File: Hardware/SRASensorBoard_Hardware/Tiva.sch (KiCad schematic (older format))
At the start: 8 parts

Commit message: Added Okis to board
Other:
- moved on the sheet: U?C, U?D, U?G, U?H
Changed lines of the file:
@@
 L MRDT_Shields:TM4C129E_Launchpad U?
 U 3 1 614D9ED3
-P 6100 2150
-F 0 "U?" H 6050 3425 60  0000 L CNN
-F 1 "TM4C129E_Launchpad" H 5625 3300 60  0000 L CNN
-F 2 "" H 6100 2150 60  0001 C CNN
-F 3 "" H 6100 2150 60  0001 C CNN
-	3    6100 2150
+P 5425 2550
+F 0 "U?" H 5375 3825 60  0000 L CNN
+F 1 "TM4C129E_Launchpad" H 4950 3700 60  0000 L CNN
+F 2 "" H 5425 2550 60  0001 C CNN
+F 3 "" H 5425 2550 60  0001 C CNN
+	3    5425 2550
 	1    0    0    -1
 $EndComp
@@
 L MRDT_Shields:TM4C129E_Launchpad U?
 U 4 1 614DBFEF
-P 7425 2175
-F 0 "U?" H 7456 3452 60  0000 C CNN
-F 1 "TM4C129E_Launchpad" H 7456 3346 60  0000 C CNN
-F 2 "" H 7425 2175 60  0001 C CNN
-F 3 "" H 7425 2175 60  0001 C CNN
-	4    7425 2175
+P 6750 2575
+F 0 "U?" H 6781 3852 60  0000 C CNN
+F 1 "TM4C129E_Launchpad" H 6781 3746 60  0000 C CNN
+F 2 "" H 6750 2575 60  0001 C CNN
+F 3 "" H 6750 2575 60  0001 C CNN
+	4    6750 2575
 	-1   0    0    -1
 $EndComp
@@
 L MRDT_Shields:TM4C129E_Launchpad U?
 U 7 1 614E25CE
-P 6200 3775
-F 0 "U?" H 6200 5100 60  0000 L CNN
-F 1 "TM4C129E_Launchpad" H 5850 4950 60  0000 L CNN
-F 2 "" H 6200 3775 60  0001 C CNN
-F 3 "" H 6200 3775 60  0001 C CNN
-	7    6200 3775
+P 5525 4175
+F 0 "U?" H 5525 5500 60  0000 L CNN
+F 1 "TM4C129E_Launchpad" H 5175 5350 60  0000 L CNN
+F 2 "" H 5525 4175 60  0001 C CNN
+F 3 "" H 5525 4175 60  0001 C CNN
+	7    5525 4175
 	1    0    0    -1
 $EndComp
@@
 L MRDT_Shields:TM4C129E_Launchpad U?
 U 8 1 614E511C
-P 7450 3775
-F 0 "U?" H 7481 5052 60  0000 C CNN
-F 1 "TM4C129E_Launchpad" H 7481 4946 60  0000 C CNN
-F 2 "" H 7450 3775 60  0001 C CNN
-F 3 "" H 7450 3775 60  0001 C CNN
-	8    7450 3775
+P 6775 4175
+F 0 "U?" H 6806 5452 60  0000 C CNN
+F 1 "TM4C129E_Launchpad" H 6806 5346 60  0000 C CNN
+F 2 "" H 6775 4175 60  0001 C CNN
+F 3 "" H 6775 4175 60  0001 C CNN
+	8    6775 4175
 	-1   0    0    -1
 $EndComp
@@
 L power:GND #PWR?
 U 1 1 614FF513
-P 7775 2825
-F 0 "#PWR?" H 7775 2575 50  0001 C CNN
-F 1 "GND" V 7780 2697 50  0000 R CNN
-F 2 "" H 7775 2825 50  0001 C CNN
-F 3 "" H 7775 2825 50  0001 C CNN
-	1    7775 2825
+P 7100 3225
+F 0 "#PWR?" H 7100 2975 50  0001 C CNN
+F 1 "GND" V 7105 3097 50  0000 R CNN
+F 2 "" H 7100 3225 50  0001 C CNN
+F 3 "" H 7100 3225 50  0001 C CNN
+	1    7100 3225
 	0    -1   -1   0
 $EndComp
@@
 L power:GND #PWR?
 U 1 1 61500297
-P 7775 1225
-F 0 "#PWR?" H 7775 975 50  0001 C CNN
-F 1 "GND" V 7780 1097 50  0000 R CNN
-F 2 "" H 7775 1225 50  0001 C CNN
-F 3 "" H 7775 1225 50  0001 C CNN
-	1    7775 1225
+P 7100 1625
+F 0 "#PWR?" H 7100 1375 50  0001 C CNN
+F 1 "GND" V 7105 1497 50  0000 R CNN
+F 2 "" H 7100 1625 50  0001 C CNN
+F 3 "" H 7100 1625 50  0001 C CNN
+	1    7100 1625
 	0    -1   -1   0
 $EndComp
@@
 $EndComp
 Wire Wire Line
-	7625 1225 7775 1225
+	6950 1625 7100 1625
 Wire Wire Line
-	7650 2825 7775 2825
+	6975 3225 7100 3225
 Wire Wire Line
 	3825 3200 3950 3200

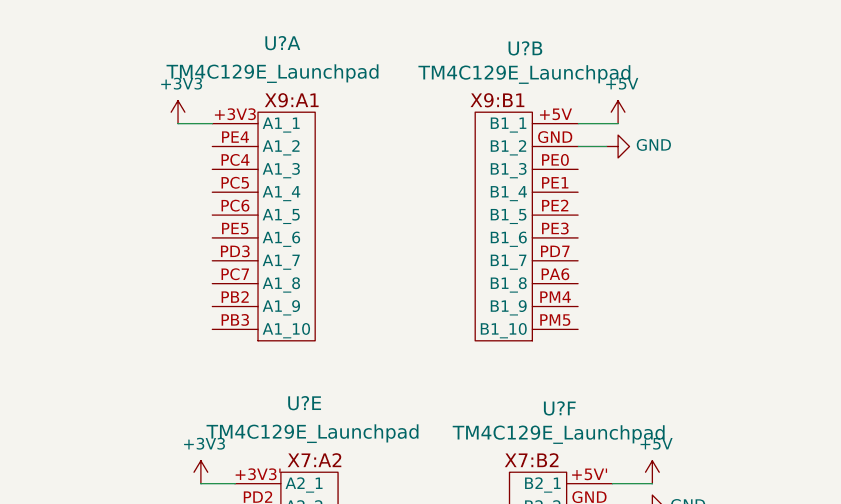
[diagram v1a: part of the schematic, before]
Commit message: Griffin_Buschjost_O2_Sensor
Copied in O2 Sensor from last year and added global labels to TIVA in pin 3 and 4 for the TIVA O2 RX and TX
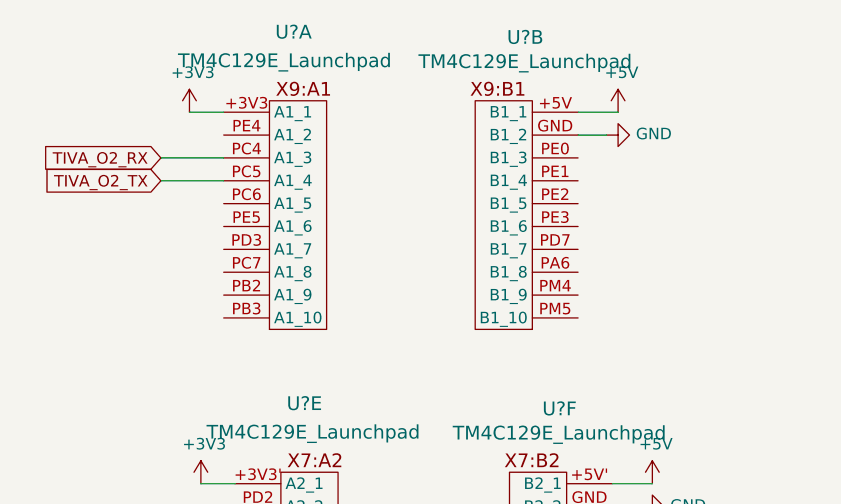
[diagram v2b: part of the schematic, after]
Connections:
- net TIVA_O2_RX: now reaches U?.PC4 (A1_3)
- net TIVA_O2_TX: now reaches U?.PC5 (A1_4)
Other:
- moved on the sheet: U?A, U?B
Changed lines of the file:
@@
 L MRDT_Shields:TM4C129E_Launchpad U?
 U 1 1 614D36F9
-P 2275 2475
-F 0 "U?" H 2300 3775 60  0000 L CNN
-F 1 "TM4C129E_Launchpad" H 1875 3650 60  0000 L CNN
-F 2 "" H 2275 2475 60  0001 C CNN
-F 3 "" H 2275 2475 60  0001 C CNN
-	1    2275 2475
+P 2325 2425
+F 0 "U?" H 2350 3725 60  0000 L CNN
+F 1 "TM4C129E_Launchpad" H 1925 3600 60  0000 L CNN
+F 2 "" H 2325 2425 60  0001 C CNN
+F 3 "" H 2325 2425 60  0001 C CNN
+	1    2325 2425
 	1    0    0    -1
 $EndComp
@@
 L MRDT_Shields:TM4C129E_Launchpad U?
 U 2 1 614D6305
-P 3475 2475
-F 0 "U?" H 3506 3752 60  0000 C CNN
-F 1 "TM4C129E_Launchpad" H 3506 3646 60  0000 C CNN
-F 2 "" H 3475 2475 60  0001 C CNN
-F 3 "" H 3475 2475 60  0001 C CNN
-	2    3475 2475
+P 3475 2425
+F 0 "U?" H 3506 3702 60  0000 C CNN
+F 1 "TM4C129E_Launchpad" H 3506 3596 60  0000 C CNN
+F 2 "" H 3475 2425 60  0001 C CNN
+F 3 "" H 3475 2425 60  0001 C CNN
+	2    3475 2425
 	-1   0    0    -1
 $EndComp
@@
 L power:GND #PWR?
 U 1 1 61500D9F
-P 3800 1625
-F 0 "#PWR?" H 3800 1375 50  0001 C CNN
-F 1 "GND" V 3805 1497 50  0000 R CNN
-F 2 "" H 3800 1625 50  0001 C CNN
-F 3 "" H 3800 1625 50  0001 C CNN
-	1    3800 1625
+P 3800 1575
+F 0 "#PWR?" H 3800 1325 50  0001 C CNN
+F 1 "GND" V 3805 1447 50  0000 R CNN
+F 2 "" H 3800 1575 50  0001 C CNN
+F 3 "" H 3800 1575 50  0001 C CNN
+	1    3800 1575
 	0    -1   -1   0
 $EndComp
@@
 	3825 3200 3950 3200
 Wire Wire Line
-	3675 1625 3800 1625
+	3675 1575 3800 1575
 $Comp
 L power:+5V #PWR?
 U 1 1 61503CB5
-P 3850 1525
-F 0 "#PWR?" H 3850 1375 50  0001 C CNN
-F 1 "+5V" H 3865 1698 50  0000 C CNN
-F 2 "" H 3850 1525 50  0001 C CNN
-F 3 "" H 3850 1525 50  0001 C CNN
-	1    3850 1525
+P 3850 1475
+F 0 "#PWR?" H 3850 1325 50  0001 C CNN
+F 1 "+5V" H 3865 1648 50  0000 C CNN
+F 2 "" H 3850 1475 50  0001 C CNN
+F 3 "" H 3850 1475 50  0001 C CNN
+	1    3850 1475
 	1    0    0    -1
 $EndComp
@@
 $EndComp
 Wire Wire Line
-	3850 1525 3675 1525
+	3850 1475 3675 1475
 Wire Wire Line
 	3825 3100 4000 3100
@@
 L power:+3V3 #PWR?
 U 1 1 61506D3B
-P 1925 1525
-F 0 "#PWR?" H 1925 1375 50  0001 C CNN
-F 1 "+3V3" H 1940 1698 50  0000 C CNN
-F 2 "" H 1925 1525 50  0001 C CNN
-F 3 "" H 1925 1525 50  0001 C CNN
-	1    1925 1525
-	1    0    0    -1
-$EndComp
-Wire Wire Line
-	1925 1525 2075 1525
+P 1975 1475
+F 0 "#PWR?" H 1975 1325 50  0001 C CNN
+F 1 "+3V3" H 1990 1648 50  0000 C CNN
+F 2 "" H 1975 1475 50  0001 C CNN
+F 3 "" H 1975 1475 50  0001 C CNN
+	1    1975 1475
+	1    0    0    -1
+$EndComp
+Wire Wire Line
+	1975 1475 2125 1475
 $Comp
 L power:+3V3 #PWR?
@@
 Wire Wire Line
 	2025 3100 2175 3100
+Text GLabel 1850 1675 0    50   Input ~ 0
+TIVA_O2_RX
+Text GLabel 1850 1775 0    50   Input ~ 0
+TIVA_O2_TX
+Wire Wire Line
+	1850 1675 2125 1675
+Wire Wire Line
+	1850 1775 2125 1775
 $EndSCHEMATC

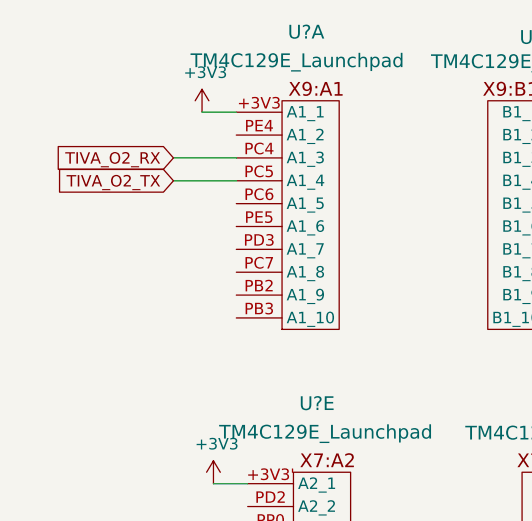
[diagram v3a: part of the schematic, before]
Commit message: added CO2 TIVA tags
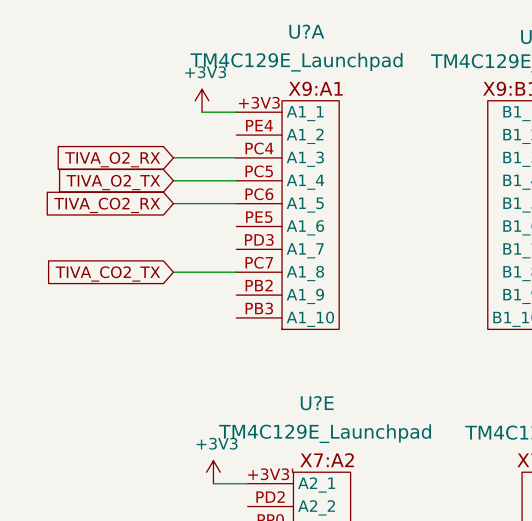
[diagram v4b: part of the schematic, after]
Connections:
- net TIVA_CO2_RX: now reaches U?.PC6 (A1_5)
- net TIVA_CO2_TX: now reaches U?.PC7 (A1_8)
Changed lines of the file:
@@
 Wire Wire Line
 	1850 1775 2125 1775
+Text GLabel 1850 2175 0    50   Input ~ 0
+TIVA_CO2_TX
+Text GLabel 1850 1875 0    50   Input ~ 0
+TIVA_CO2_RX
+Wire Wire Line
+	2125 1875 1850 1875
+Wire Wire Line
+	2125 2175 1850 2175
 $EndSCHEMATC

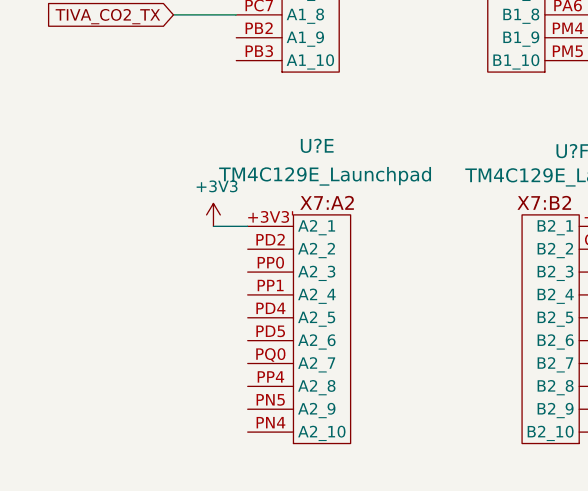
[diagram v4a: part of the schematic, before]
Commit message: Methane Sensor & Tiva Pins added
Added USB A connector and USB to UART converter for CH4 sensor
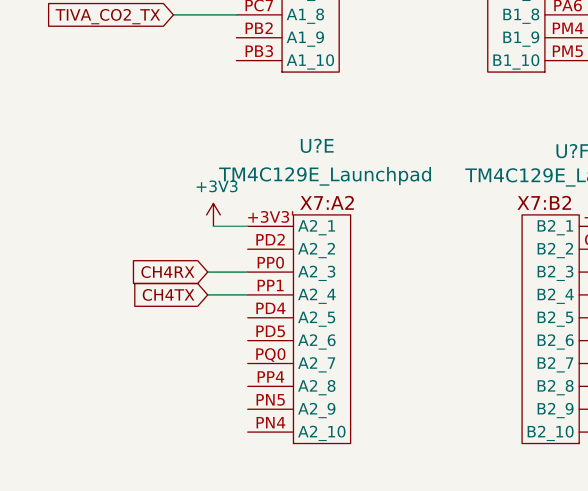
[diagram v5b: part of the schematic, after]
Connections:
- net CH4RX: now reaches U?.PP0 (A2_3)
- net CH4TX: now reaches U?.PP1 (A2_4)
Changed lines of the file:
@@
 Wire Wire Line
 	2125 2175 1850 2175
+Text GLabel 2000 3300 0    50   Input ~ 0
+CH4RX
+Text GLabel 2000 3400 0    50   Input ~ 0
+CH4TX
+Wire Wire Line
+	2000 3300 2175 3300
+Wire Wire Line
+	2000 3400 2175 3400
 $EndSCHEMATC

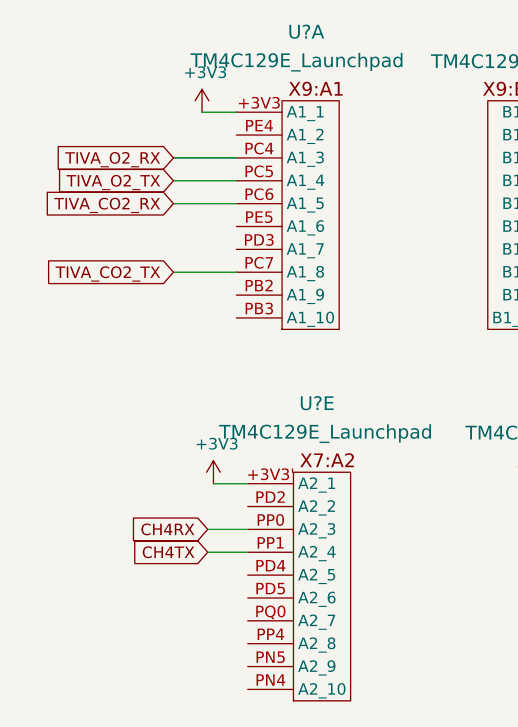
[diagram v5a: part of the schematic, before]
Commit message: Renamed CH4 RX/TX to match with others, swapped tx&rx tiva pins (might be wrong)
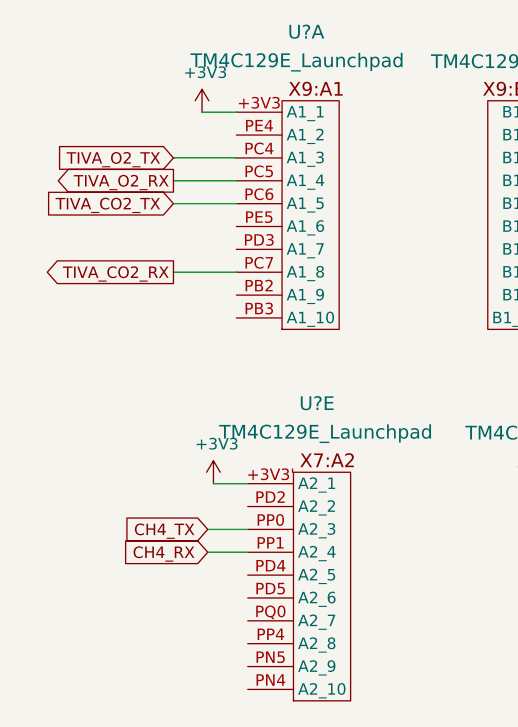
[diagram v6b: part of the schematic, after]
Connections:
- net TIVA_CO2_RX: now also U?.PC7 (A1_8); no longer U?.PC6 (A1_5)
- net TIVA_CO2_TX: now also U?.PC6 (A1_5); no longer U?.PC7 (A1_8)
- net TIVA_O2_RX: now also U?.PC5 (A1_4); no longer U?.PC4 (A1_3)
- net TIVA_O2_TX: now also U?.PC4 (A1_3); no longer U?.PC5 (A1_4)
- net CH4RX renamed CH4_TX
- net CH4TX renamed CH4_RX
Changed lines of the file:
@@
 Wire Wire Line
 	2025 3100 2175 3100
+Text GLabel 1850 1775 0    50   Output ~ 0
+TIVA_O2_RX
 Text GLabel 1850 1675 0    50   Input ~ 0
-TIVA_O2_RX
-Text GLabel 1850 1775 0    50   Input ~ 0
 TIVA_O2_TX
 Wire Wire Line
@@
 Wire Wire Line
 	1850 1775 2125 1775
-Text GLabel 1850 2175 0    50   Input ~ 0
+Text GLabel 1850 1875 0    50   Input ~ 0
 TIVA_CO2_TX
-Text GLabel 1850 1875 0    50   Input ~ 0
+Text GLabel 1850 2175 0    50   Output ~ 0
 TIVA_CO2_RX
 Wire Wire Line
@@
 Wire Wire Line
 	2125 2175 1850 2175
+Text GLabel 2000 3400 0    50   Input ~ 0
+CH4_RX
 Text GLabel 2000 3300 0    50   Input ~ 0
-CH4RX
-Text GLabel 2000 3400 0    50   Input ~ 0
-CH4TX
+CH4_TX
 Wire Wire Line
 	2000 3300 2175 3300

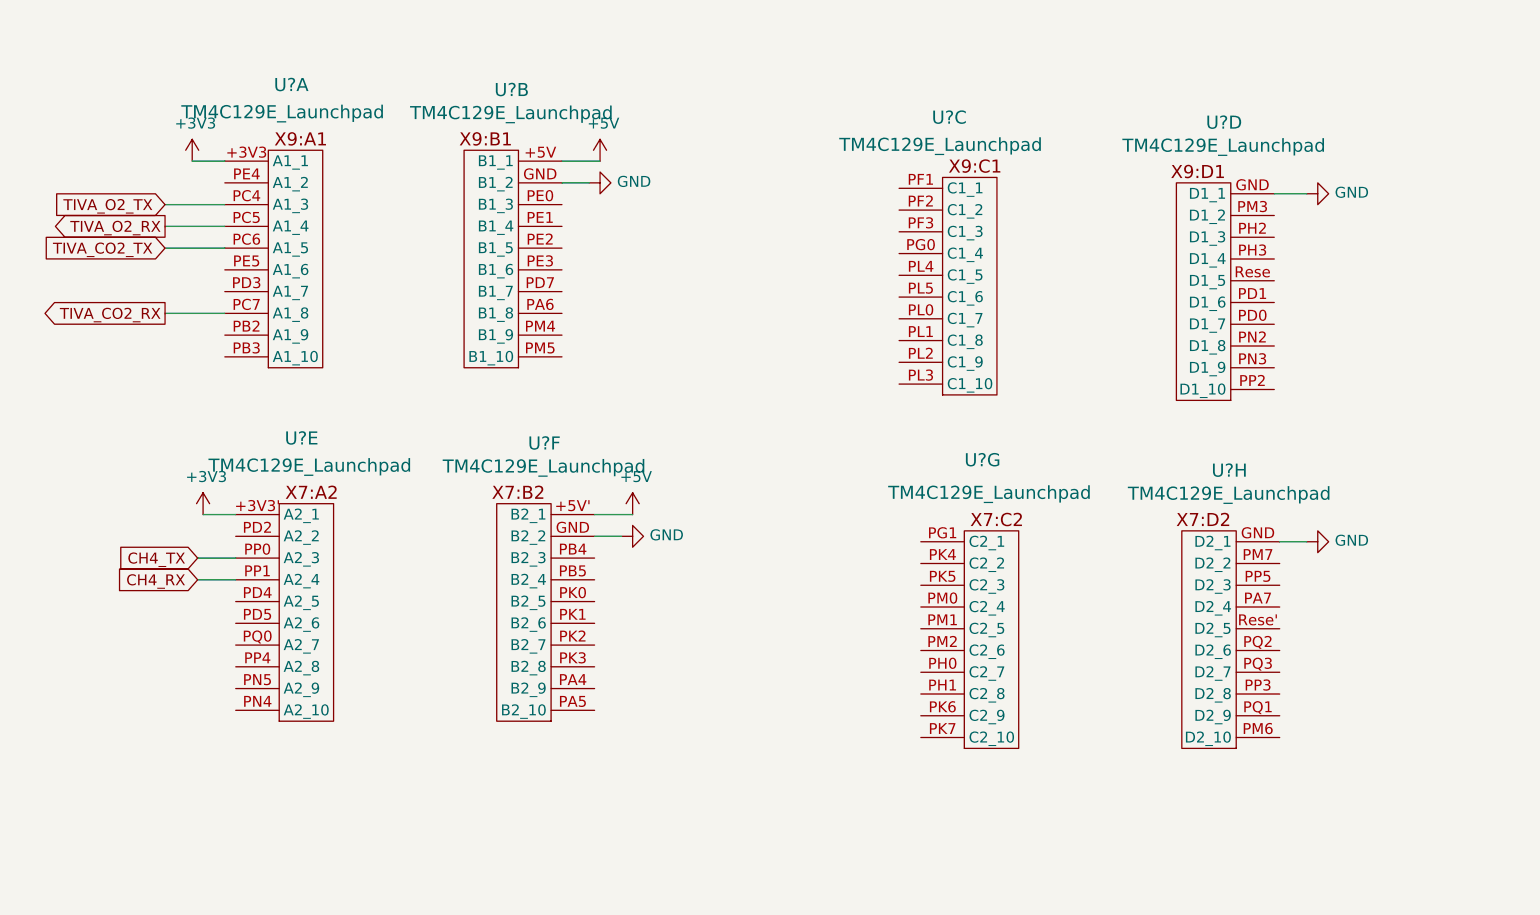
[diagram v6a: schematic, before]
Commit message: Added NH3 sensor and MOSFETS, fixed tiva pins
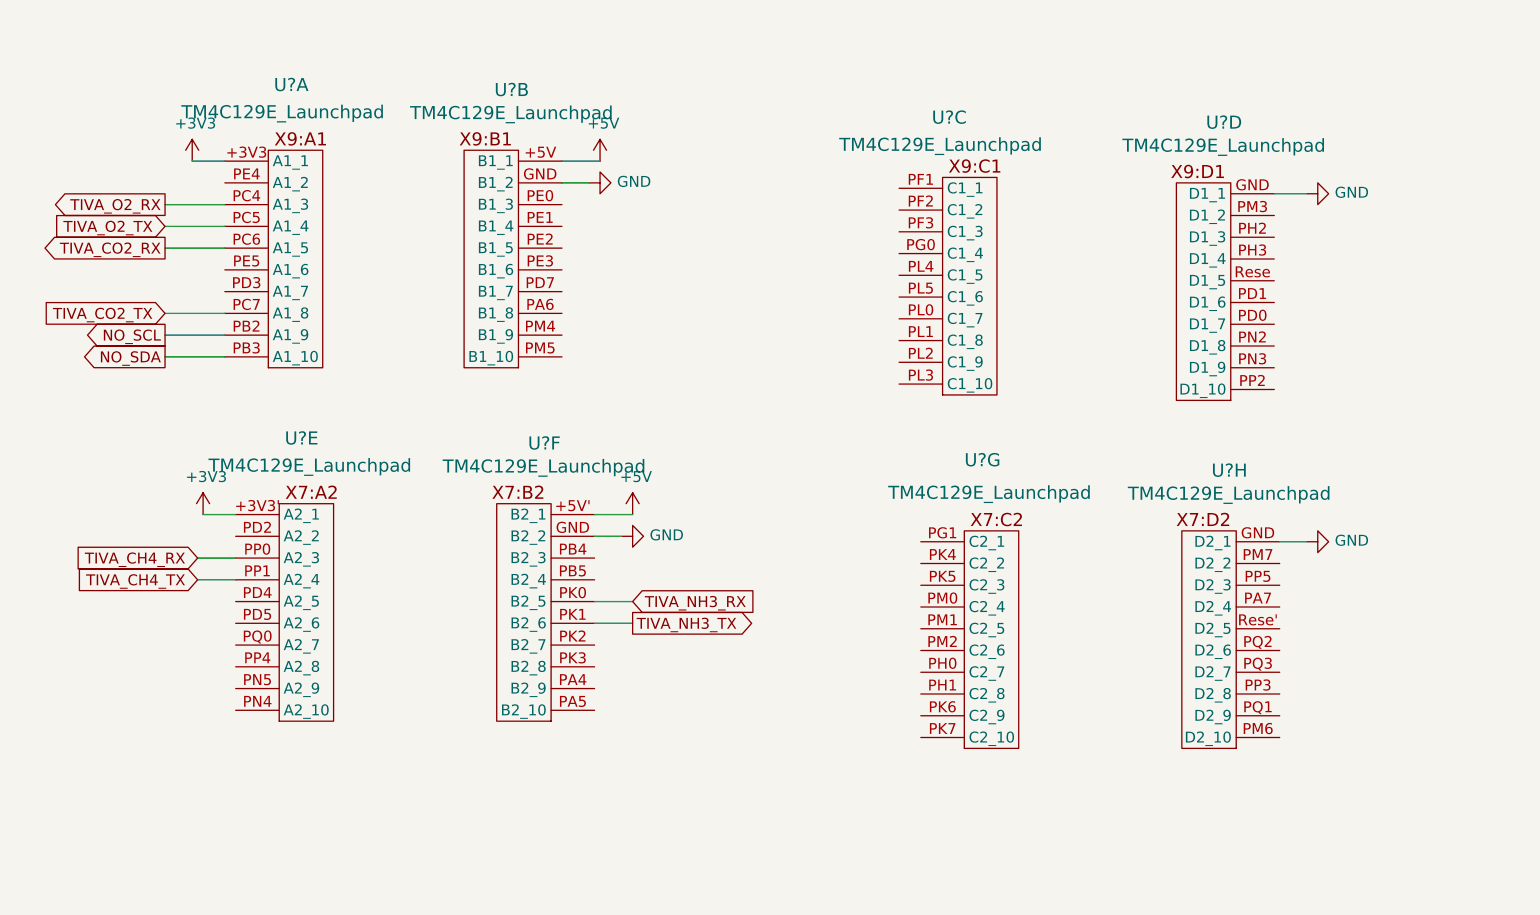
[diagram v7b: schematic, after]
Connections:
- net TIVA_CO2_RX: now also U?.PC6 (A1_5); no longer U?.PC7 (A1_8)
- net TIVA_CO2_TX: now also U?.PC7 (A1_8); no longer U?.PC6 (A1_5)
- net TIVA_O2_RX: now also U?.PC4 (A1_3); no longer U?.PC5 (A1_4)
- net TIVA_O2_TX: now also U?.PC5 (A1_4); no longer U?.PC4 (A1_3)
- net NO_SCL: now reaches U?.PB2 (A1_9)
- net NO_SDA: now reaches U?.PB3 (A1_10)
- net TIVA_NH3_RX: now reaches U?.PK0 (B2_5)
- net TIVA_NH3_TX: now reaches U?.PK1 (B2_6)
- net CH4_RX renamed TIVA_CH4_TX
- net CH4_TX renamed TIVA_CH4_RX
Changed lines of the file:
@@
 Wire Wire Line
 	2025 3100 2175 3100
-Text GLabel 1850 1775 0    50   Output ~ 0
+Text GLabel 1850 1675 0    50   Output ~ 0
 TIVA_O2_RX
-Text GLabel 1850 1675 0    50   Input ~ 0
+Text GLabel 1850 1775 0    50   Input ~ 0
 TIVA_O2_TX
 Wire Wire Line
@@
 Wire Wire Line
 	1850 1775 2125 1775
-Text GLabel 1850 1875 0    50   Input ~ 0
+Text GLabel 1850 2175 0    50   Input ~ 0
 TIVA_CO2_TX
-Text GLabel 1850 2175 0    50   Output ~ 0
+Text GLabel 1850 1875 0    50   Output ~ 0
 TIVA_CO2_RX
 Wire Wire Line
@@
 Wire Wire Line
 	2125 2175 1850 2175
+Text GLabel 2000 3300 0    50   Input ~ 0
+TIVA_CH4_RX
 Text GLabel 2000 3400 0    50   Input ~ 0
-CH4_RX
-Text GLabel 2000 3300 0    50   Input ~ 0
-CH4_TX
+TIVA_CH4_TX
 Wire Wire Line
 	2000 3300 2175 3300
 Wire Wire Line
 	2000 3400 2175 3400
+Text GLabel 1850 2275 0    50   Output ~ 0
+NO_SCL
+Text GLabel 1850 2375 0    50   Output ~ 0
+NO_SDA
+Wire Wire Line
+	2125 2275 1850 2275
+Wire Wire Line
+	2125 2375 1850 2375
+Text GLabel 4000 3500 2    50   Input ~ 0
+TIVA_NH3_RX
+Text GLabel 4000 3600 2    50   Output ~ 0
+TIVA_NH3_TX
+Wire Wire Line
+	4000 3500 3825 3500
+Wire Wire Line
+	3825 3600 4000 3600
 $EndSCHEMATC
